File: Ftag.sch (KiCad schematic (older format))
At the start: 24 parts, among them CON1 USB-MINI-B, U1 FT232H, X1 12 MHz

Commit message: Added note about experimental feature
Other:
- note added: "EXPERIMENTAL!\nDo not populate!"
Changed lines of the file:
@@
 Sheet 1 1
 Title "Ftag"
-Date "16 jul 2015"
+Date "13 sep 2015"
 Rev "V 1.0"
 Comp ""
@@
 Wire Wire Line
 	5500 1550 5600 1550
+Wire Notes Line
+	4200 1250 6000 1250
+Wire Notes Line
+	6000 1250 6000 2900
+Wire Notes Line
+	6000 2900 4200 2900
+Wire Notes Line
+	4200 2900 4200 1250
+Text Notes 4500 2450 0    60   ~ 0
+EXPERIMENTAL!\nDo not populate!
 $EndSCHEMATC

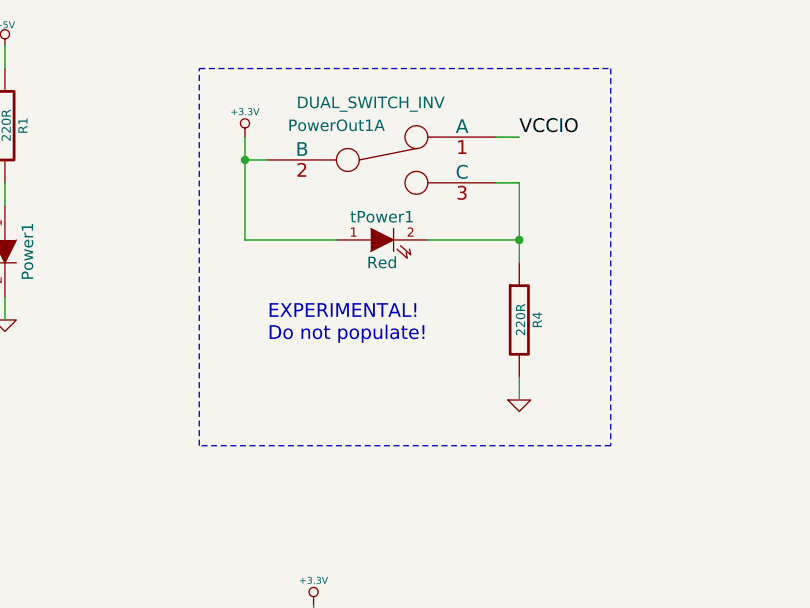
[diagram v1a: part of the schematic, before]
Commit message: removed experimental parts
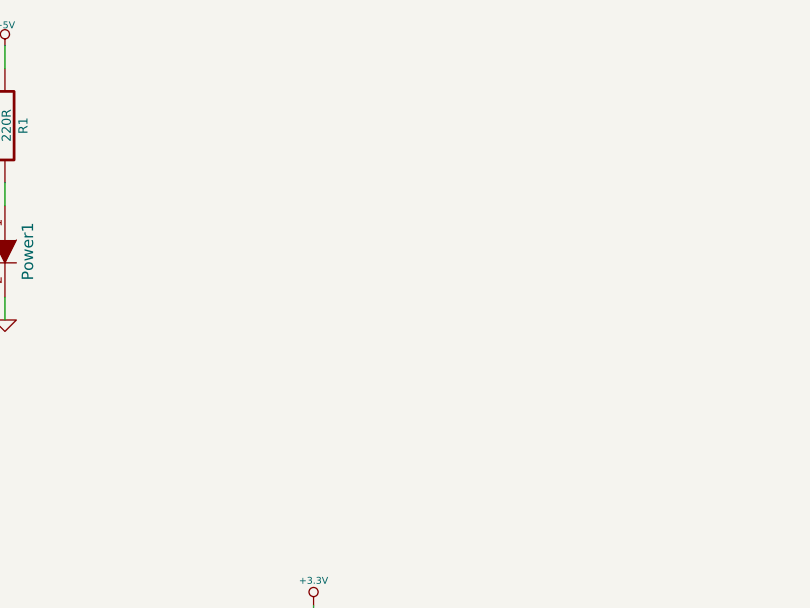
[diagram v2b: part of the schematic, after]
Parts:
- removed PowerOut1: DUAL_SWITCH_INV, ~, symbol DUAL_SWITCH_INV
- removed R4: 220R, ~, symbol R
- removed tPower1: Red, ~, symbol LED
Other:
- note removed: "EXPERIMENTAL!\nDo not populate!"
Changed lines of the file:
@@
 Sheet 1 1
 Title "Ftag"
-Date "13 sep 2015"
+Date "27 nov 2015"
 Rev "V 1.0"
 Comp ""
@@
 RI/RTCK/
 $Comp
-L DUAL_SWITCH_INV PowerOut1
-U 1 1 53FD3F2B
-P 5000 1650
-F 0 "PowerOut1" H 4800 1800 50  0000 C CNN
-F 1 "DUAL_SWITCH_INV" H 4950 1900 50  0000 C CNN
-F 2 "~" H 5000 1650 60  0000 C CNN
-F 3 "~" H 5000 1650 60  0000 C CNN
-	1    5000 1650
-	1    0    0    -1
-$EndComp
-$Comp
 L +5V #PWR016
 U 1 1 53FD3F38
@@
 	1    0    0    -1
 $EndComp
-$Comp
-L +3.3V #PWR018
-U 1 1 53FD4199
-P 4400 1550
-F 0 "#PWR018" H 4400 1510 30  0001 C CNN
-F 1 "+3.3V" H 4400 1660 30  0000 C CNN
-F 2 "" H 4400 1550 60  0000 C CNN
-F 3 "" H 4400 1550 60  0000 C CNN
-	1    4400 1550
-	1    0    0    -1
-$EndComp
-Text Label 5600 1550 0    60   ~ 0
-VCCIO
 Text Label 5750 5000 0    60   ~ 0
 TRST
@@
 NoConn ~ 8800 5500
 NoConn ~ 8800 5600
-$Comp
-L LED tPower1
-U 1 1 53FDFDA1
-P 5000 2000
-F 0 "tPower1" H 5000 2100 50  0000 C CNN
-F 1 "Red" H 5000 1900 50  0000 C CNN
-F 2 "~" H 5000 2000 60  0000 C CNN
-F 3 "~" H 5000 2000 60  0000 C CNN
-	1    5000 2000
-	1    0    0    -1
-$EndComp
-$Comp
-L R R4
-U 1 1 53FDFED6
-P 5600 2350
-F 0 "R4" V 5680 2350 40  0000 C CNN
-F 1 "220R" V 5607 2351 40  0000 C CNN
-F 2 "~" V 5530 2350 30  0000 C CNN
-F 3 "~" H 5600 2350 30  0000 C CNN
-	1    5600 2350
-	1    0    0    -1
-$EndComp
-$Comp
-L GND #PWR019
-U 1 1 53FDFEE5
-P 5600 2700
-F 0 "#PWR019" H 5600 2700 30  0001 C CNN
-F 1 "GND" H 5600 2630 30  0001 C CNN
-F 2 "" H 5600 2700 60  0000 C CNN
-F 3 "" H 5600 2700 60  0000 C CNN
-	1    5600 2700
-	1    0    0    -1
-$EndComp
 Text Label 8200 4900 0    60   ~ 0
 RX/TDI/DO
@@
 	5650 5600 5750 5600
 Wire Wire Line
-	5600 2600 5600 2700
-Connection ~ 5600 2000
-Wire Wire Line
-	5600 1750 5500 1750
-Wire Wire Line
-	5600 1750 5600 2100
-Wire Wire Line
-	5200 2000 5600 2000
-Connection ~ 4400 1650
-Wire Wire Line
-	4400 2000 4800 2000
-Wire Wire Line
-	4400 1650 4500 1650
-Wire Wire Line
-	4400 1550 4400 2000
-Wire Wire Line
 	3350 2250 3350 2350
 Wire Wire Line
@@
 	9000 4400 9000 4500
 Connection ~ 9000 4500
-Wire Wire Line
-	5500 1550 5600 1550
-Wire Notes Line
-	4200 1250 6000 1250
-Wire Notes Line
-	6000 1250 6000 2900
-Wire Notes Line
-	6000 2900 4200 2900
-Wire Notes Line
-	4200 2900 4200 1250
-Text Notes 4500 2450 0    60   ~ 0
-EXPERIMENTAL!\nDo not populate!
 $EndSCHEMATC

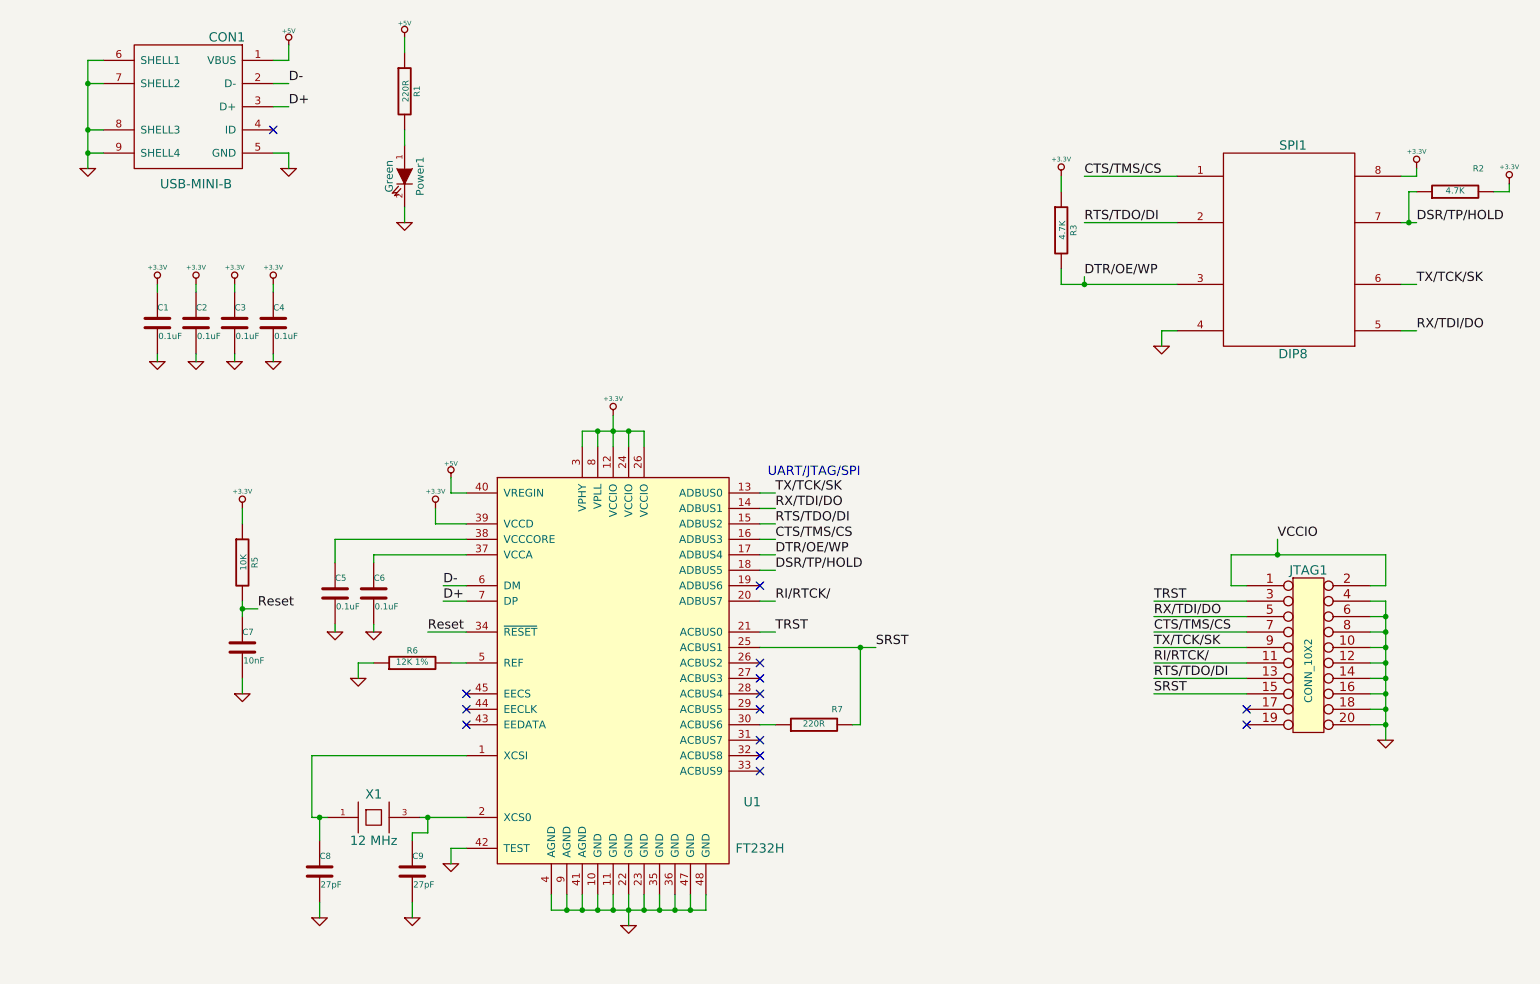
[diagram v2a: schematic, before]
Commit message: Added output buffer
Some things still have to be checked before adding part footprints
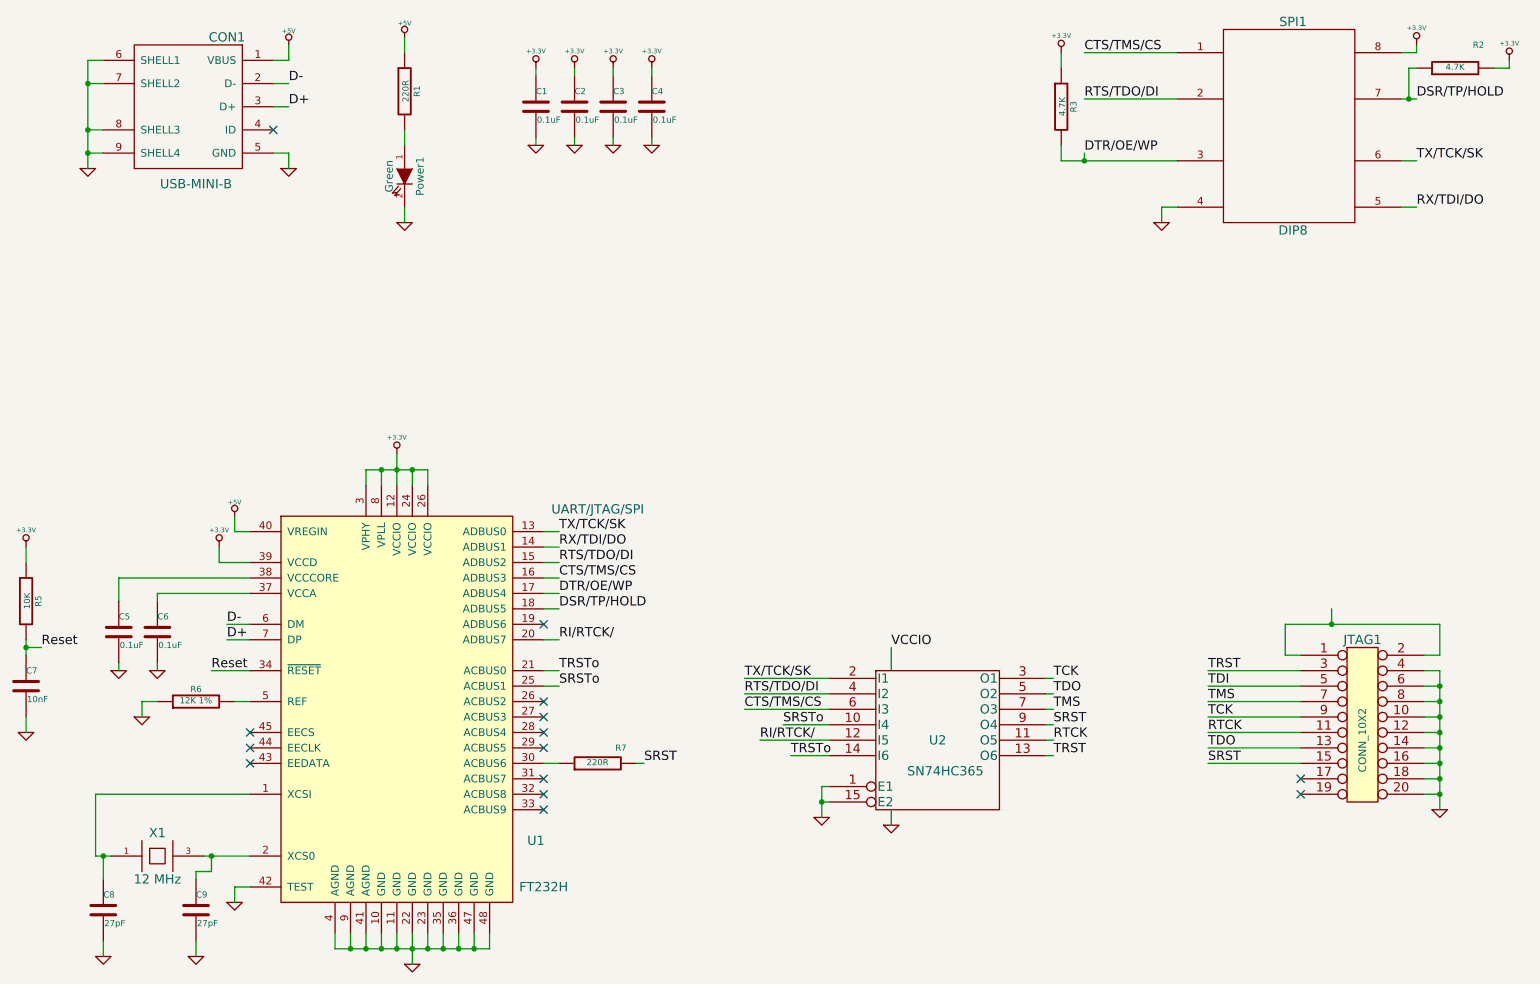
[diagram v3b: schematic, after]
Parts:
- added U2: SN74HC365, ~, symbol 74LS365
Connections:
- net CTS/TMS/CS: now also U2.6 (I3); no longer JTAG1.7 (P7)
- net GND: now also U2.1 (E1), U2.15 (E2), U2.8 (GND)
- net RI/RTCK/: now also U2.12 (I5); no longer JTAG1.11 (P11)
- net RTS/TDO/DI: now also U2.4 (I2); no longer JTAG1.13 (P13)
- net RX/TDI/DO: no longer JTAG1.5 (P5)
- net SRST: now also U2.9 (O4); no longer U1.25 (ACBUS1)
- net TRST: now also U2.13 (O6); no longer U1.21 (ACBUS0)
- net TX/TCK/SK: now also U2.2 (I1); no longer JTAG1.9 (P9)
- net VCCIO: no longer names the net of JTAG1.1 (P1), JTAG1.2 (P2)
- new net RTCK: JTAG1.11 (P11), U2.11 (O5)
- new net SRSTo: U1.25 (ACBUS1), U2.10 (I4)
- new net TCK: JTAG1.9 (P9), U2.3 (O1)
- new net TDI: JTAG1.5 (P5)
- new net TDO: JTAG1.13 (P13), U2.5 (O2)
- new net TMS: JTAG1.7 (P7), U2.7 (O3)
- new net TRSTo: U1.21 (ACBUS0), U2.14 (I6)
- new net VCC: U2.16 (VCC)
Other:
- moved on the sheet: C1, C2, C3, C4, C5, C6, C7, C8, C9, JTAG1, R2, R3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
